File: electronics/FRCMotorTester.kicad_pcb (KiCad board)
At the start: 2 copper layers, 89 parts, among them J1 USB_B_Micro, J2 Conn_01x02_Socket, J5 Conn_01x02_Socket, Q2 IRLML6401, SW1 PTS645SK50SMTR92LFS, SW2 RotaryEncoder_Switch, SW3 RotaryEncoder_Switch, U1 W25Q32JVZP, U2 RP2040, U3 MCP25625T-E/ML, U4 ANT13SECQE, U5 LM1117DT-ADJ, U6 AOZ1280CI, U7 LM1117DT-ADJ, Y1 Crystal, Y2 8MHz

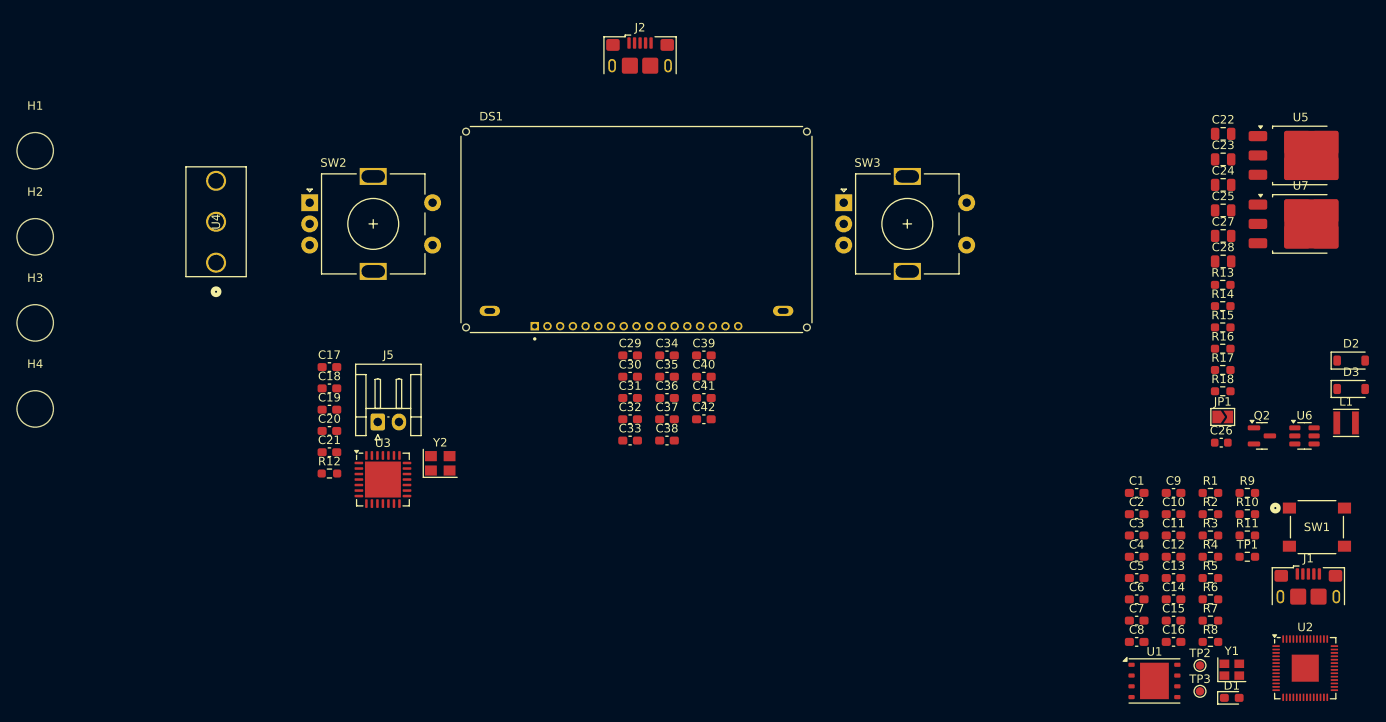
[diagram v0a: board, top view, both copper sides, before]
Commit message: Many changes to the design. Fully routed.
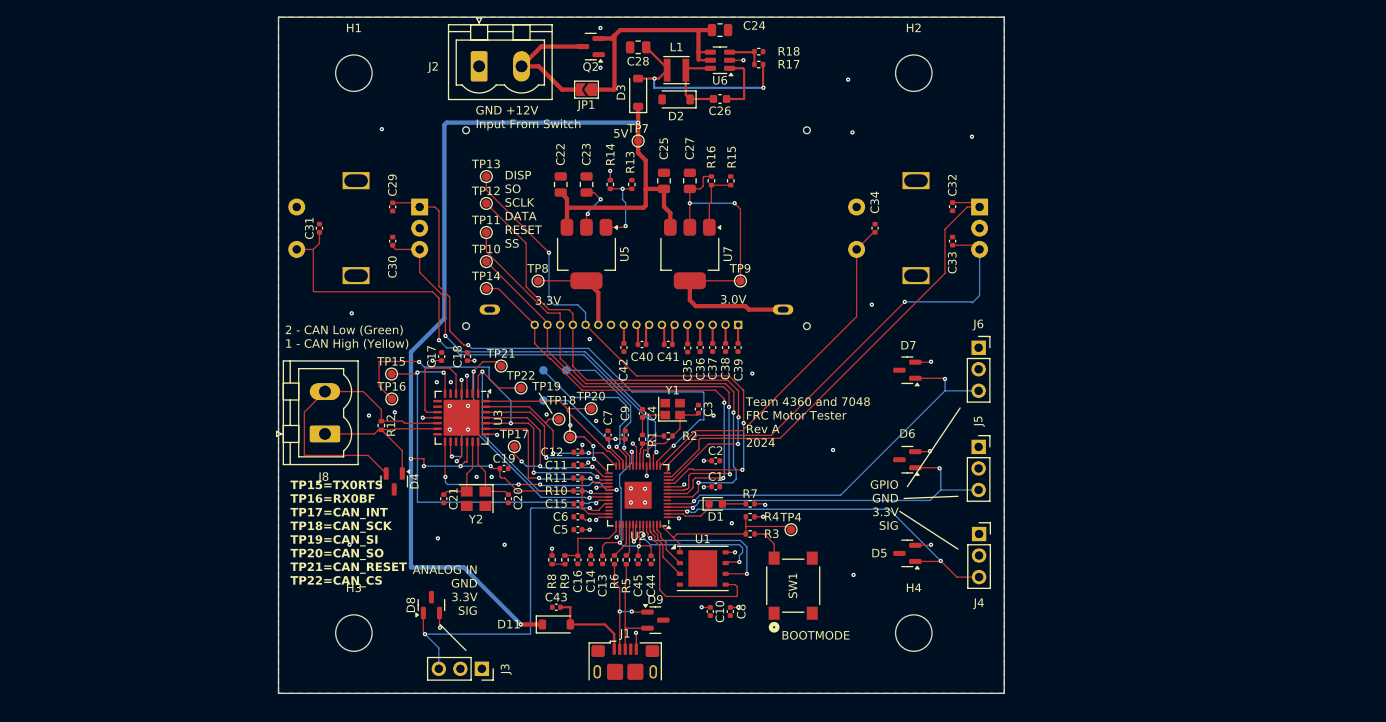
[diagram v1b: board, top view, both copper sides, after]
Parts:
- removed U4: ANT13SECQE, footprints:ANT13SEC_CRS
- added C43: 2.2u, Capacitor_SMD:C_0402_1005Metric, F.Cu at (122.9, 105.7)
- added C44: 0.1u, Capacitor_SMD:C_0402_1005Metric, F.Cu at (134.1, 100.1)
- added C45: 0.1u, Capacitor_SMD:C_0402_1005Metric, F.Cu at (132.6, 100.1)
- added D11: D_Schottky, Diode_SMD:D_SOD-123, F.Cu at (122.9, 107.7)
- added D4: SP0502BAHT, Package_TO_SOT_SMD:SOT-23, F.Cu at (103.8, 90.8)
- added D5: SP0502BAHT, Package_TO_SOT_SMD:SOT-23, F.Cu at (164.3, 99.3)
- added D6: SP0502BAHT, Package_TO_SOT_SMD:SOT-23, F.Cu at (164.3, 88.3)
- added D7: SP0502BAHT, Package_TO_SOT_SMD:SOT-23, F.Cu at (164.3, 77.7)
- added D8: SP0502BAHT, Package_TO_SOT_SMD:SOT-23, F.Cu at (108.2, 105.4)
- added D9: SP0502BAHT, Package_TO_SOT_SMD:SOT-23, F.Cu at (134.6, 107.2)
- added J3: Conn_01x03, Connector_PinSocket_2.54mm:PinSocket_1x03_P2.54mm_Vertical, F.Cu at (114.2, 112.9)
- added J4: Conn_01x03, Connector_PinSocket_2.54mm:PinSocket_1x03_P2.54mm_Vertical, F.Cu at (172.8, 97.0)
- added J6: Conn_01x03, Connector_PinSocket_2.54mm:PinSocket_1x03_P2.54mm_Vertical, F.Cu at (172.7, 75.1)
- added J8: Conn_01x02, Connector_Phoenix_MSTB:PhoenixContact_MSTBVA_2,5_2-G_1x02_P5.00mm_Vertical, F.Cu at (95.6, 85.2)
- added TP10: TestPoint, TestPoint:TestPoint_Pad_D1.0mm, F.Cu at (114.7, 64.9)
- added TP11: TestPoint, TestPoint:TestPoint_Pad_D1.0mm, F.Cu at (114.7, 61.5)
- added TP12: TestPoint, TestPoint:TestPoint_Pad_D1.0mm, F.Cu at (114.7, 58.0)
- added TP13: TestPoint, TestPoint:TestPoint_Pad_D1.0mm, F.Cu at (114.7, 54.9)
- added TP14: TestPoint, TestPoint:TestPoint_Pad_D1.0mm, F.Cu at (114.7, 68.1)
- added TP15: TestPoint, TestPoint:TestPoint_Pad_D1.0mm, F.Cu at (103.5, 78.2)
- added TP16: TestPoint, TestPoint:TestPoint_Pad_D1.0mm, F.Cu at (103.5, 81.1)
- added TP17: TestPoint, TestPoint:TestPoint_Pad_D1.0mm, F.Cu at (118.0, 86.7)
- added TP18: TestPoint, TestPoint:TestPoint_Pad_D1.0mm, F.Cu at (124.6, 85.6)
- added TP19: TestPoint, TestPoint:TestPoint_Pad_D1.0mm, F.Cu at (123.2, 83.5)
- added TP20: TestPoint, TestPoint:TestPoint_Pad_D1.0mm, F.Cu at (127.1, 82.2)
- added TP21: TestPoint, TestPoint:TestPoint_Pad_D1.0mm, F.Cu at (116.4, 77.2)
- added TP22: TestPoint, TestPoint:TestPoint_Pad_D1.0mm, F.Cu at (118.8, 79.8)
- added TP4: TestPoint, TestPoint:TestPoint_Pad_D1.0mm, F.Cu at (150.6, 96.5)
- added TP7: TestPoint, TestPoint:TestPoint_Pad_D1.0mm, F.Cu at (132.6, 50.7)
- added TP8: TestPoint, TestPoint:TestPoint_Pad_D1.0mm, F.Cu at (120.8, 67.2)
- added TP9: TestPoint, TestPoint:TestPoint_Pad_D1.0mm, F.Cu at (144.7, 67.2)
- C1, C10, C11, C12, C15, C17, C18, C19, C2, C20, C21, C29, C3, C30, C31, C32, C33, C34, C35, C36, C37, C38, C39, C4, C40, C41, C42, C5, C6, C7, C8, C9: footprint Capacitor_SMD:C_0603_1608Metric_Pad1.08x0.95mm_HandSolder -> Capacitor_SMD:C_0402_1005Metric
- C13, C14, C16: value 2.2u -> 1u; footprint Capacitor_SMD:C_0603_1608Metric_Pad1.08x0.95mm_HandSolder -> Capacitor_SMD:C_0402_1005Metric
- D1: footprint LED_SMD:LED_0603_1608Metric_Pad1.05x0.95mm_HandSolder -> LED_SMD:LED_0603_1608Metric
- DS1, SW2, SW3, TP2, TP3: moved to B.Cu
- J2: footprint Connector_USB:USB_Micro-B_Amphenol_10118193-0001LF_Horizontal -> Connector_Phoenix_MSTB:PhoenixContact_MSTBVA_2,5_2-G_1x02_P5.00mm_Vertical
- J5: value Conn_01x02_Socket -> Conn_01x03; footprint Connector_JST:JST_EH_S2B-EH_1x02_P2.50mm_Horizontal -> Connector_PinSocket_2.54mm:PinSocket_1x03_P2.54mm_Vertical
- R1, R10, R11, R12, R13, R14, R15, R16, R17, R18, R2, R3, R4, R5, R6, R7, R8, R9: footprint Resistor_SMD:R_0603_1608Metric_Pad0.98x0.95mm_HandSolder -> Resistor_SMD:R_0402_1005Metric
- TP1: footprint Resistor_SMD:R_0603_1608Metric_Pad0.98x0.95mm_HandSolder -> TestPoint:TestPoint_Pad_D1.0mm; moved to B.Cu
- U5, U7: footprint Package_TO_SOT_SMD:TO-252-3_TabPin2 -> Package_TO_SOT_SMD:SOT-223-3_TabPin2
- moved H4 107.0 mm to (165.1, 108.7)
- moved H2 105.4 mm to (165.1, 42.7)
- moved Q2 91.5 mm to (127.0, 39.5), turned to 180 degrees
- moved D3 91.1 mm to (132.6, 45.0), turned to 90 degrees
- moved L1 89.3 mm to (137.1, 42.3), turned to 180 degrees
- moved TP1 85.9 mm to (121.4, 77.7)
- moved D2 85.4 mm to (137.1, 45.8), turned to 180 degrees
- moved U5 85.0 mm to (126.5, 64.0), turned to -90 degrees
- moved TP3 84.7 mm to (121.4, 81.3)
- moved JP1 84.4 mm to (126.5, 44.6), turned to 180 degrees
- moved TP2 82.5 mm to (124.1, 77.7)
- moved U6 81.9 mm to (142.2, 41.1), turned to 180 degrees
- moved U2 81.3 mm to (132.6, 92.5), turned to 180 degrees
- moved J1 81.1 mm to (131.1, 113.3)
- moved R9 80.9 mm to (124.0, 100.1), turned to 90 degrees
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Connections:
- C13 pad 1: 3V3 -> +1V1
- J1 pad 1: VCC -> Net-(D11-A)
- J2 pad 2: Net-(J2-Pin_2) -> /Power/VIN
- J5 pad 1: Net-(J5-Pin_1) -> GND
- J5 pad 2: Net-(J5-Pin_2) -> 3V3
- R12 pad 1: Net-(J5-Pin_2) -> Net-(J8-Pin_2)
- R12 pad 2: Net-(J5-Pin_1) -> Net-(J8-Pin_1)
- U2 pad 23: 3V3 -> +1V1
- U2 pad 3: unconnected-(U2-GPIO1-Pad3) -> GENIO_01
- U2 pad 38: unconnected-(U2-GPIO26_ADC0-Pad38) -> ANALOG_IN
- U2 pad 4: unconnected-(U2-GPIO2-Pad4) -> GENIO_02
- U2 pad 45: 3V3 -> +1V1
- U2 pad 5: unconnected-(U2-GPIO3-Pad5) -> GENIO_03
- U2 pad 50: 3V3 -> +1V1
- U2 pad 6: MAIN_ENABLE -> unconnected-(U2-GPIO4-Pad6)
- U3 pad 12: Net-(J5-Pin_2) -> Net-(J8-Pin_2)
- U3 pad 13: Net-(J5-Pin_1) -> Net-(J8-Pin_1)
- Y2 pad 1: Net-(U3-OSC2) -> Net-(U3-OSC1)
- Y2 pad 2: Net-(U3-OSC1) -> Net-(U3-OSC2)
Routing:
- net VCC: track 0.00 -> 153.2 mm, vias 0 -> 6
- net DISP_SO: track 0.00 -> 65.0 mm, vias 0 -> 3
- net ENC1A: track 0.00 -> 64.8 mm, vias 0 -> 2
- net PRESS1: track 0.00 -> 63.5 mm, vias 0 -> 2
- net DISP_SCLK: track 0.00 -> 61.9 mm, vias 0 -> 2
- net 3V3: track 0.00 -> 61.9 mm, vias 0 -> 32
- net DISP_DATA: track 0.00 -> 61.4 mm, vias 0 -> 2
- net ENC2A: track 0.00 -> 57.1 mm
- net DISP_RESET: track 0.00 -> 55.7 mm, vias 0 -> 2
- net ENC2B: track 0.00 -> 55.0 mm, vias 0 -> 1
- net DISP_SS: track 0.00 -> 52.0 mm, vias 0 -> 2
- net ENC1B: track 0.00 -> 49.3 mm, vias 0 -> 2
- net GENIO_03: track 0.00 -> 47.2 mm, vias 0 -> 2
- net TX0RTS: track 0.00 -> 47.0 mm, vias 0 -> 3
- net RX0BF: track 0.00 -> 46.3 mm, vias 0 -> 4
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- added copper zone on In2.Cu, net 3V3
- added copper zone on B.Cu, net GND
- added copper zone on F.Cu, net GND
- added copper zone on In1.Cu, net GND
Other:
- board outline added: 85.6 x 79.8 mm
- copper layers 2 -> 4
- board text added: "2 - CAN Low (Green) 1 - CAN High (Yellow)"
- board text added: "3.0V"
- board text added: "3.3V"
- board text added: "5V"
- board text added: "ANALOG IN GND 3.3V SIG"
- board text added: "BOOTMODE"
- board text added: "DISP SO SCLK DATA RESET SS"
- board text added: "GND +12V Input From Switch"
- board text added: "GPIO GND 3.3V SIG"
- board text added: "TP15=TX0RTS TP16=RX0BF TP17=CAN_INT TP18=CAN_SCK TP19=CAN_SI TP20=CAN_SO TP21=CAN_RESET TP22=CAN_CS"
- board text added: "Team 4360 and 7048 FRC Motor Tester Rev A 2024"

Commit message: Almost sent this to fab. It is getting expensive.
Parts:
- Y2: value 8MHz -> 20MHz

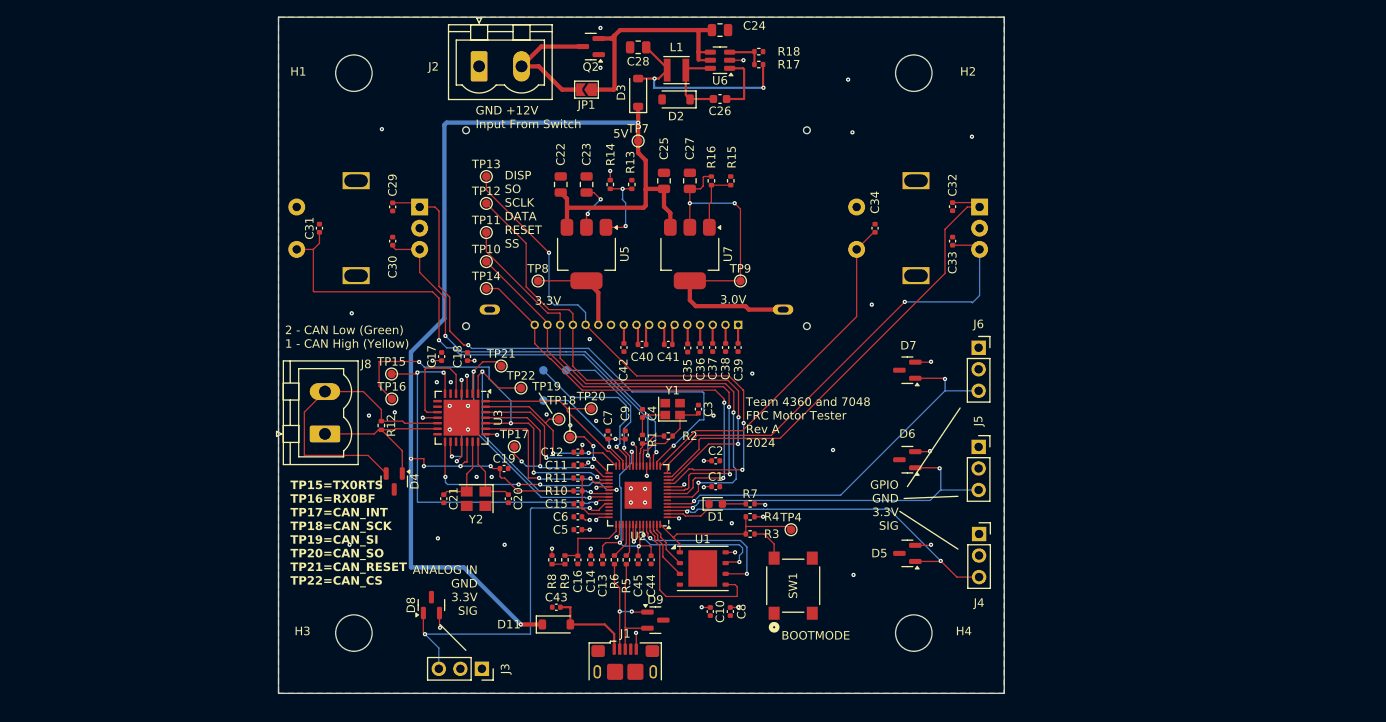
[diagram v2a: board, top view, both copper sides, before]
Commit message: Switched processor.
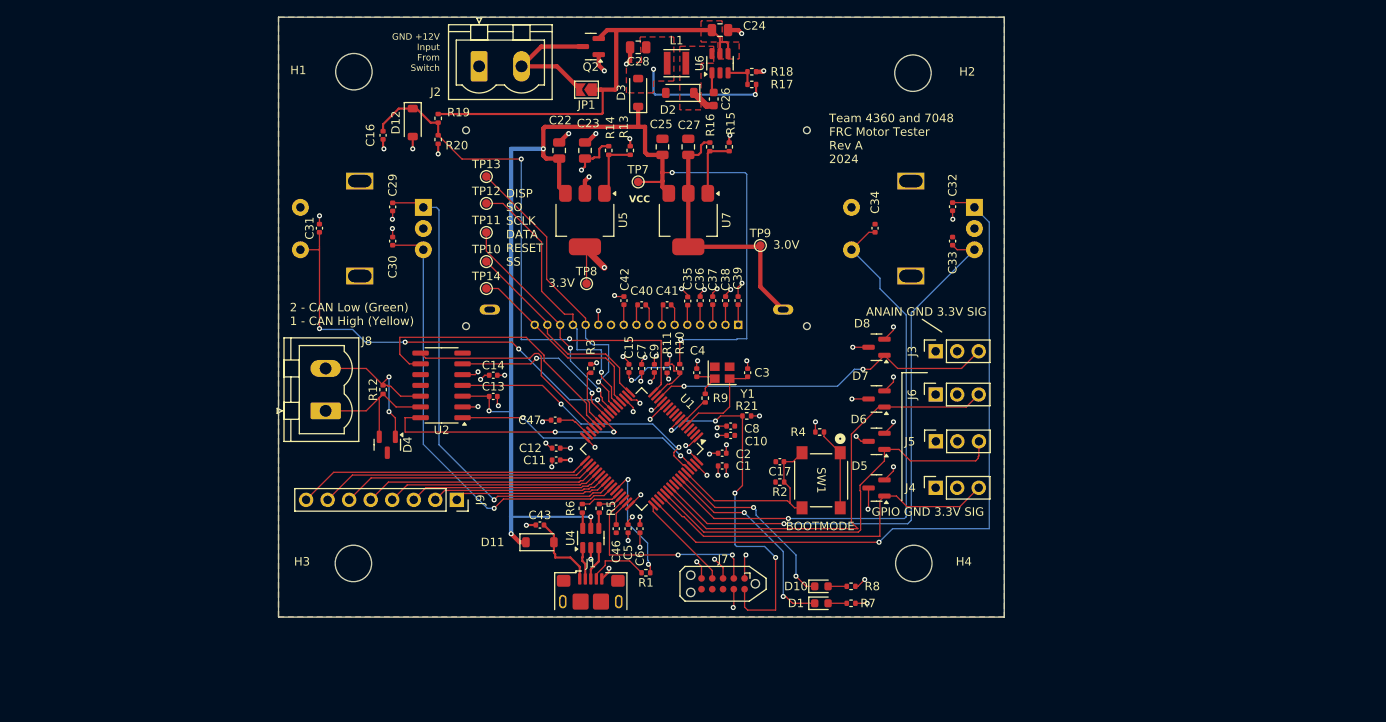
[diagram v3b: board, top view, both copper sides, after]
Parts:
- removed C18, C19, C44, C45: 0.1u, Capacitor_SMD:C_0402_1005Metric
- removed C20, C21: 22p, Capacitor_SMD:C_0402_1005Metric
- removed D9: SP0502BAHT, Package_TO_SOT_SMD:SOT-23
- removed TP1, TP15, TP16, TP17, TP18, TP19, TP2, TP20, TP21, TP22, TP3, TP4: TestPoint, TestPoint:TestPoint_Pad_D1.0mm
- removed U3: MCP25625T-E/ML, Package_DFN_QFN:QFN-28-1EP_6x6mm_P0.65mm_EP4.25x4.25mm
- removed Y2: 20MHz, Crystal:Crystal_SMD_3225-4Pin_3.2x2.5mm
- added C46: 2.2u, Capacitor_SMD:C_0402_1005Metric, F.Cu at (130.0, 96.4)
- added C47: 2.2u, Capacitor_SMD:C_0402_1005Metric, F.Cu at (122.8, 83.6)
- added D10: LED, LED_SMD:LED_0603_1608Metric, F.Cu at (154.2, 103.2)
- added D12: D_Zener, Diode_SMD:D_SOD-123, F.Cu at (106.0, 48.5)
- added J7: Conn_ARM_JTAG_SWD_10, Connector:Tag-Connect_TC2050-IDC-NL_2x05_P1.27mm_Vertical_with_bottom_clip, F.Cu at (142.6, 102.9)
- added J9: Conn_01x08, Connector_PinSocket_2.54mm:PinSocket_1x08_P2.54mm_Vertical, F.Cu at (111.2, 93.0)
- added R19: 100k, Resistor_SMD:R_0402_1005Metric, F.Cu at (109.0, 48.0)
- added R20: 10k, Resistor_SMD:R_0402_1005Metric, F.Cu at (109.0, 50.5)
- added R21: 4.7k, Resistor_SMD:R_0402_1005Metric, F.Cu at (145.4, 83.1)
- added U4: USBLC6-2SC6, Package_TO_SOT_SMD:SOT-23-6, F.Cu at (127.0, 97.5)
- C1: value 0.1u -> 4.7u
- C13, C14: value 1u -> 0.1u
- C15: value 2.2u -> 1u
- C8: value 2.2u -> 0.1u
- R1: value 1k -> 560
- R10: value 200k -> 20k
- R11: value 100k -> 10k
- R2: value DNP -> 100k
- R3: value 1K -> 100k
- R4: value DNP -> 1K
- R5, R6: value 27 -> 22
- R8: value 200R -> 330
- R9: value 1R -> 1K
- U1: value W25Q32JVZP -> STM32F415RGTx; footprint Package_SON:WSON-8-1EP_6x5mm_P1.27mm_EP3.4x4.3mm -> Package_QFP:LQFP-64_10x10mm_P0.5mm
- U2: value RP2040 -> TCAN1043xDxQ1; footprint Package_DFN_QFN:QFN-56-1EP_7x7mm_P0.4mm_EP3.2x3.2mm -> Package_SO:SOIC-14_3.9x8.7mm_P1.27mm
- moved J3 65.3 mm to (167.7, 75.5), turned to 90 degrees
- moved D8 60.7 mm to (160.7, 75.0), turned to 180 degrees
- moved C16 55.1 mm to (102.5, 50.0)
- moved C17 41.8 mm to (149.3, 88.5), turned to 180 degrees
- moved R8 35.4 mm to (157.7, 103.2), turned to 0 degrees
- moved R3 27.1 mm to (127.0, 77.5), turned to 90 degrees
- moved U2 26.6 mm to (109.4, 79.5)
- moved R9 25.3 mm to (140.5, 81.0)
- moved C14 24.6 mm to (115.5, 78.3), turned to 0 degrees
- moved C13 23.2 mm to (115.5, 80.8), turned to 0 degrees
- moved C8 21.9 mm to (143.5, 84.3), turned to 0 degrees
- moved C10 20.9 mm to (143.5, 85.4), turned to 0 degrees
- moved R10 18.8 mm to (137.5, 77.5), turned to -90 degrees
- moved D1 17.1 mm to (154.2, 105.2)
- moved C15 17.1 mm to (131.5, 77.5), turned to 90 degrees
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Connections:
- C13 pad 1: +1V1 -> VCC
- C15 pad 1: Net-(U2-GPIO29_ADC3) -> VCC_MEAS
- C16 pad 1: Net-(U2-ADC_AVDD) -> VIN_MEAS
- C17 pad 1: 3V3 -> /Pico/BOOT
- C3 pad 2: Net-(U2-XIN) -> /Pico/OSC_IN
- C4 pad 2: Net-(C4-Pad2) -> /Pico/OSC_OUT
- D1 pad 1: Net-(D1-K) -> LED1
- D4 pad 1: Net-(J8-Pin_1) -> Net-(J8-Pin_2)
- D4 pad 2: Net-(J8-Pin_2) -> Net-(J8-Pin_1)
- J1 pad 4: unconnected-(J1-ID-Pad4) -> Net-(J1-ID)
- R1 pad 1: Net-(C4-Pad2) -> ID
- R1 pad 2: Net-(U2-XOUT) -> Net-(J1-ID)
- R10 pad 2: Net-(U2-GPIO29_ADC3) -> VCC_MEAS
- R11 pad 1: Net-(U2-GPIO29_ADC3) -> VCC_MEAS
- R12 pad 1: Net-(J8-Pin_2) -> Net-(J8-Pin_1)
- R12 pad 2: Net-(J8-Pin_1) -> Net-(J8-Pin_2)
- R2 pad 1: Net-(U2-XIN) -> /Pico/BOOT
- R2 pad 2: Net-(U2-XOUT) -> GND
- R3 pad 1: Net-(R3-Pad1) -> Net-(U1-PB1)
- R3 pad 2: /Pico/QSPI_SS -> GND
- R4 pad 2: /Pico/QSPI_SS -> Net-(R4-Pad2)
- R5 pad 1: Net-(J1-D+) -> Net-(R5-Pad1)
- R5 pad 2: Net-(U2-USB_DP) -> DP
- R6 pad 1: Net-(J1-D-) -> Net-(R6-Pad1)
- R6 pad 2: Net-(U2-USB_DM) -> DM
- R8 pad 1: 3V3 -> Net-(D10-A)
- R8 pad 2: /Pico/ADC_VREF -> 3V3
- R9 pad 1: /Pico/ADC_VREF -> Net-(U1-PH1)
- R9 pad 2: Net-(U2-ADC_AVDD) -> /Pico/OSC_OUT
- SW1 pad 1: unconnected-(SW1-Pad1) -> Net-(R4-Pad2)
- SW1 pad 2: Net-(R3-Pad1) -> Net-(R4-Pad2)
- SW1 pad 3: GND -> /Pico/BOOT
- SW1 pad 4: GND -> /Pico/BOOT
- U1 pad 1: /Pico/QSPI_SS -> 3V3
- U1 pad 2: Net-(U1-DO(IO1)) -> unconnected-(U1-PC13-Pad2)
- U1 pad 3: Net-(U1-IO2) -> unconnected-(U1-PC14-Pad3)
- U1 pad 4: GND -> unconnected-(U1-PC15-Pad4)
- U1 pad 5: Net-(U1-DI(IO0)) -> /Pico/OSC_IN
- U1 pad 6: Net-(U1-CLK) -> Net-(U1-PH1)
- U1 pad 7: Net-(U1-IO3) -> NRST
- U1 pad 8: 3V3 -> unconnected-(U1-PC0-Pad8)
- U1 pad 9: GND -> unconnected-(U1-PC1-Pad9)
- U2 pad 1: 3V3 -> CAN_TX
- U2 pad 10: 3V3 -> unconnected-(U2-VSUP-Pad10)
- U2 pad 11: DISP_SO -> unconnected-(U2-NC-Pad11)
- U2 pad 12: DISP_SCLK -> Net-(J8-Pin_2)
- U2 pad 13: ENC2A -> Net-(J8-Pin_1)
- U2 pad 14: ENC2B -> CAN_STB
- U2 pad 2: Net-(D1-K) -> GND
- U2 pad 3: GENIO_01 -> VCC
- U2 pad 4: GENIO_02 -> CAN_RX
- U2 pad 5: GENIO_03 -> 3V3
- U2 pad 6: unconnected-(U2-GPIO4-Pad6) -> CAN_EN
- U2 pad 7: DISP_DATA -> unconnected-(U2-INH-Pad7)
- U2 pad 8: DISP_SS -> CAN_FAULT
- U2 pad 9: DISP_RESET -> CAN_WAKE
- Y1 pad 1: Net-(C4-Pad2) -> /Pico/OSC_OUT
- Y1 pad 2: Net-(U2-XIN) -> /Pico/OSC_IN
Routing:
- net VIN_MEAS: track 0.00 -> 65.7 mm, vias 0 -> 2
- net GND: track 8.64 -> 71.2 mm, vias 39 -> 51
- net TX0RTS: track 47.0 -> 0.00 mm, vias 3 -> 0
- net RX0BF: track 46.3 -> 0.00 mm, vias 4 -> 0
- net NRST: track 0.00 -> 44.0 mm, vias 0 -> 4
- net SPARE8: track 0.00 -> 34.9 mm
- net DISP_DATA: track 61.4 -> 27.1 mm
- net CAN_WAKE: track 0.00 -> 33.7 mm
- net CAN_CS: track 33.4 -> 0.00 mm, vias 2 -> 0
- net CAN_RESET: track 32.8 -> 0.00 mm, vias 2 -> 0
- net SPARE7: track 0.00 -> 32.5 mm
- net CAN_RX: track 0.00 -> 32.3 mm, vias 0 -> 2
- net CAN_STB: track 0.00 -> 30.9 mm, vias 0 -> 2
- net DISP_RESET: track 55.7 -> 25.1 mm, vias 2 -> 0
- net SPARE6: track 0.00 -> 30.2 mm
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- added copper zone on F.Cu, net +12V
- added copper zone on F.Cu, net Net-(D2-K)
- added copper zone on F.Cu, net Net-(D3-A)
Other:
- board size 85.6 x 79.8 mm -> 85.6 x 70.8 mm
- board text added: "ANAIN GND 3.3V SIG"
- board text added: "VCC"
- board text removed: "5V"
- board text removed: "ANALOG IN GND 3.3V SIG"
- board text removed: "TP15=TX0RTS TP16=RX0BF TP17=CAN_INT TP18=CAN_SCK TP19=CAN_SI TP20=CAN_SO TP21=CAN_RESET TP22=CAN_CS"

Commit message: Ordered this version.
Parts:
- removed Y1: Crystal, Crystal:Crystal_SMD_2520-4Pin_2.5x2.0mm
- added Y2: Crystal_GND24, Crystal:Crystal_SMD_3225-4Pin_3.2x2.5mm, F.Cu at (142.4, 77.7)
- C1: footprint Capacitor_SMD:C_0402_1005Metric -> Capacitor_SMD:C_0805_2012Metric
- C40, C41, C42, C43, C46, C47: footprint Capacitor_SMD:C_0402_1005Metric -> Capacitor_SMD:C_0603_1608Metric
- R1: footprint Resistor_SMD:R_0402_1005Metric -> Resistor_SMD:R_0603_1608Metric
- moved C41 3.30 mm to (135.9, 66.7)
- moved C42 1.71 mm to (129.7, 68.3)
- moved C5 0.90 mm to (132.3, 96.4)
- moved D11 0.90 mm to (121.0, 98.9)
- moved C6 0.90 mm to (133.7, 96.4)
- moved C46 0.67 mm to (130.6, 96.7)
- moved C1 0.64 mm to (143.0, 89.4)
- moved C3 0.60 mm to (146.1, 78.0)
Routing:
- net Net-(DS1-C2+): track 2.41 -> 5.84 mm
- net /Pico/OSC_IN: track 11.6 -> 14.8 mm
- net Net-(DS1-C2-): track 2.53 -> 5.68 mm
- net GND: track 71.2 -> 74.1 mm
- net Net-(DS1-VOUT): track 2.39 -> 3.60 mm
- net VCC: track 146.9 -> 148.1 mm
- net ID: track 14.2 -> 15.3 mm
- net 3V3: track 57.9 -> 58.9 mm
- net Net-(D11-A): track 9.16 -> 8.64 mm
